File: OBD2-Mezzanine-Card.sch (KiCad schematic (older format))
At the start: 60 parts, among them IC1 ELM327, J1 OBD2-DB9_Male, P1 CONN_02X20, Q1 2N3904, Q2 2N3906, Q3 2N3906, Q4 2N3904, Q5 2N3904, Q6 2N3904, Q7 2N3904, U1 MCP2561-E/P, U2 LM317L_TO92, Y1 4.0MHz

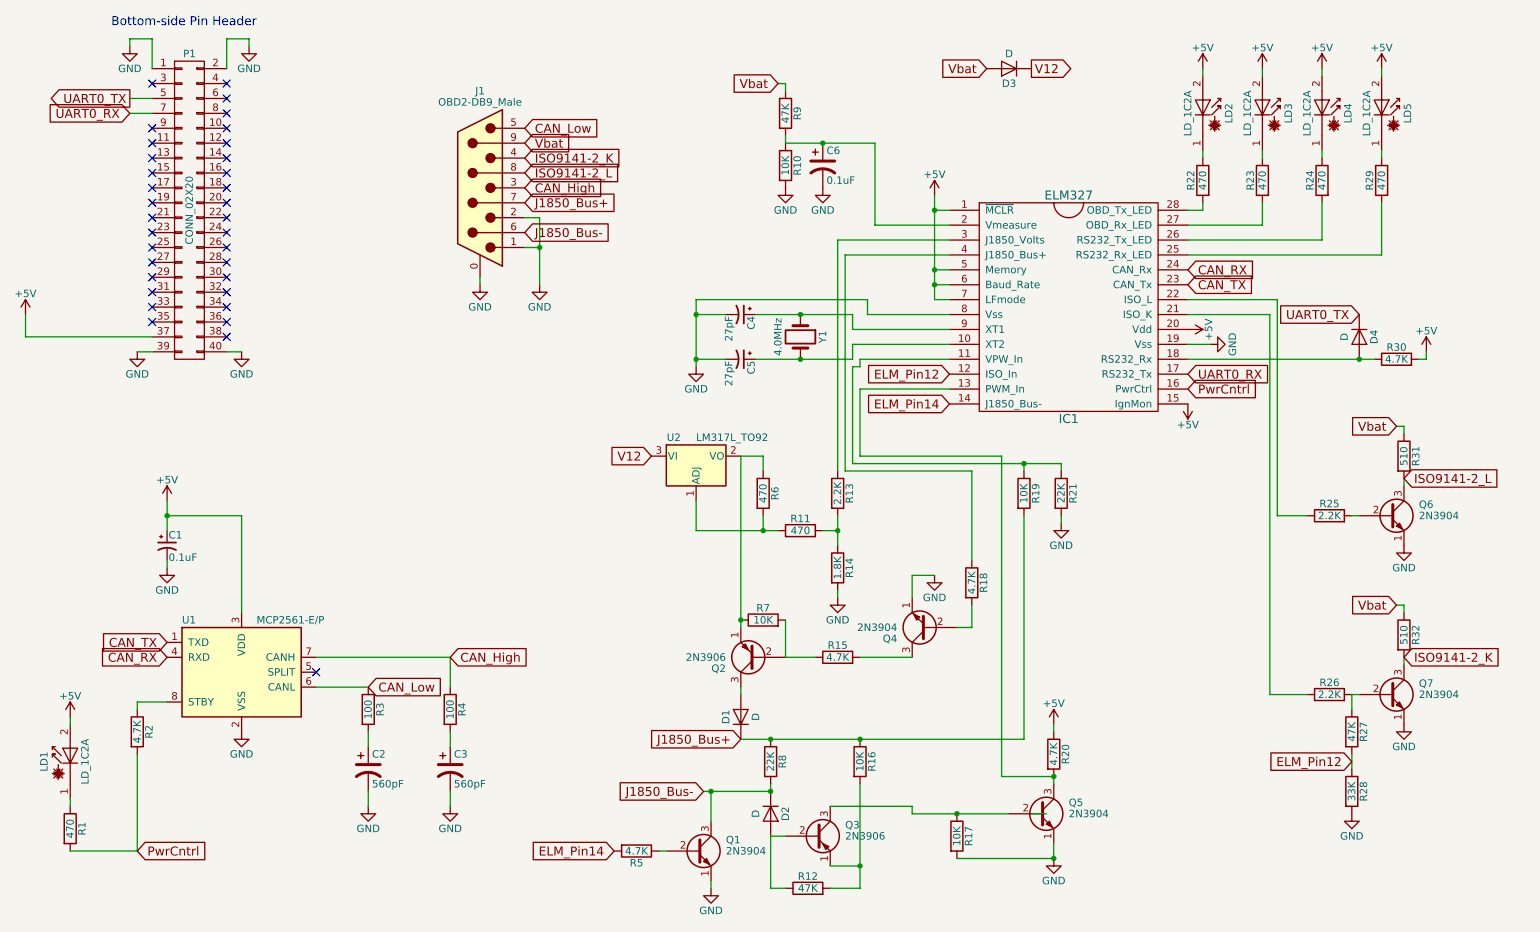
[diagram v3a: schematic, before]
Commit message: sch: Pass all electrical checks and add some lables
Schematic is ready for review.

Signed-off-by: Alistair Francis <alistair@alistair23.me>
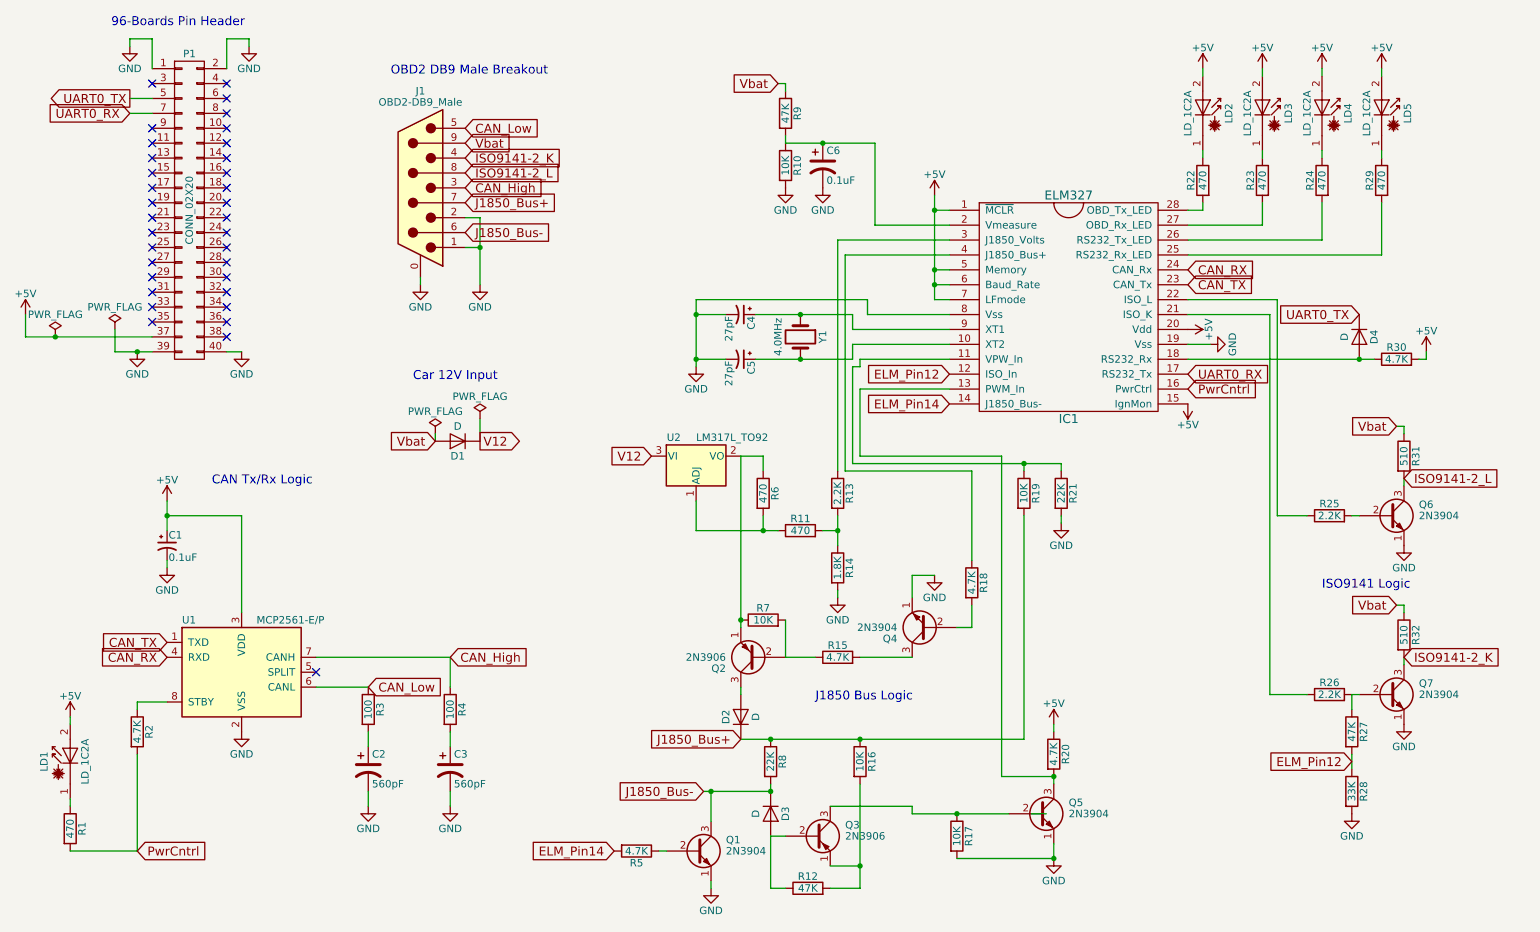
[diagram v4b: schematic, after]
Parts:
- renumbered D3 to D1, D1 to D2, D2 to D3
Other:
- note added: "96-Boards Pin Header"
- note added: "CAN Tx/Rx Logic\n"
- note added: "Car 12V Input\n"
- note added: "ISO9141 Logic\n"
- note added: "J1850 Bus Logic\n"
- note added: "OBD2 DB9 Male Breakout\n"
- note removed: "Bottom-side Pin Header"
- moved on the sheet: D1, J1

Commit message: sch: Add PCB footprints to most parts
Signed-off-by: Alistair Francis <alistair@alistair23.me>
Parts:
- C1, C2, C3, C4, C5, C6: footprint (none) -> Capacitors_SMD:C_0603_HandSoldering
- D1, D2, D3, D4: footprint (none) -> Diodes_SMD:D_SOD-123
- IC1: footprint (none) -> Pin_Headers:Pin_Header_Straight_1x28_Pitch2.54mm
- LD1, LD2, LD3, LD4, LD5: footprint (none) -> Opto-Devices:LaserDiode_TO5(D9)-3
- R1, R11, R22, R23, R24, R29, R3, R31, R32, R4, R6: footprint (none) -> Resistors_SMD:R_0603_HandSoldering
- R10, R12, R16, R17, R19, R21, R27, R28, R7, R8, R9: footprint (none) -> Resistors_SMD:R_1206_HandSoldering
- R13, R14, R15, R18, R2, R20, R25, R26, R30, R5: footprint (none) -> Resistors_SMD:R_0201
- Y1: footprint (none) -> Crystals:Crystal_HC49-U_Vertical

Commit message: sch: Finalise the PCB footprints
Signed-off-by: Alistair Francis <alistair@alistair23.me>
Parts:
- J1: footprint (none) -> Connectors_DSub:DSUB-9_Male_Horizontal_Pitch2.77x2.84mm_EdgePinOffset4.94mm_Housed_MountingHolesOffset7.48mm
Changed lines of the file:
@@
 F 0 "J1" H 3350 2450 50  0000 C CNN
 F 1 "OBD2-DB9_Male" H 3350 2375 50  0000 C CNN
-F 2 "" H 3350 1800 50  0001 C CNN
+F 2 "Connectors_DSub:DSUB-9_Male_Horizontal_Pitch2.77x2.84mm_EdgePinOffset4.94mm_Housed_MountingHolesOffset7.48mm" H 3350 1800 50  0001 C CNN
 F 3 "" H 3350 1800 50  0001 C CNN
 	1    3350 1800

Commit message: sch: Fix up the some PCB footprints
Signed-off-by: Alistair Francis <alistair@alistair23.me>
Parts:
- IC1: footprint Pin_Headers:Pin_Header_Straight_1x28_Pitch2.54mm -> Housings_DIP:DIP-28_W7.62mm
- LD1, LD2, LD3, LD4, LD5: footprint Opto-Devices:LaserDiode_TO5(D9)-3 -> Opto-Devices:LaserDiode_TO3.3(D3.3)-3
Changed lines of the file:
@@
 F 0 "IC1" H 7700 1850 60  0000 C CNN
 F 1 "ELM327" H 7700 3350 60  0000 C CNN
-F 2 "Pin_Headers:Pin_Header_Straight_1x28_Pitch2.54mm" H 7700 3350 60  0001 C CNN
+F 2 "Housings_DIP:DIP-28_W7.62mm" H 7700 3350 60  0001 C CNN
 F 3 "" H 7700 3350 60  0001 C CNN
 	1    7700 2600
@@
 F 0 "LD2" H 8550 1425 50  0000 C CNN
 F 1 "LD_1C2A" H 8550 1150 50  0000 C CNN
-F 2 "Opto-Devices:LaserDiode_TO5(D9)-3" H 8500 1225 50  0001 C CNN
+F 2 "Opto-Devices:LaserDiode_TO3.3(D3.3)-3" H 8500 1225 50  0001 C CNN
 F 3 "" H 8630 1050 50  0001 C CNN
 	1    8600 1250
@@
 F 0 "LD3" H 8950 1425 50  0000 C CNN
 F 1 "LD_1C2A" H 8950 1150 50  0000 C CNN
-F 2 "Opto-Devices:LaserDiode_TO5(D9)-3" H 8900 1225 50  0001 C CNN
+F 2 "Opto-Devices:LaserDiode_TO3.3(D3.3)-3" H 8900 1225 50  0001 C CNN
 F 3 "" H 9030 1050 50  0001 C CNN
 	1    9000 1250
@@
 F 0 "LD4" H 9350 1425 50  0000 C CNN
 F 1 "LD_1C2A" H 9350 1150 50  0000 C CNN
-F 2 "Opto-Devices:LaserDiode_TO5(D9)-3" H 9300 1225 50  0001 C CNN
+F 2 "Opto-Devices:LaserDiode_TO3.3(D3.3)-3" H 9300 1225 50  0001 C CNN
 F 3 "" H 9430 1050 50  0001 C CNN
 	1    9400 1250
@@
 F 0 "LD5" H 9750 1425 50  0000 C CNN
 F 1 "LD_1C2A" H 9750 1150 50  0000 C CNN
-F 2 "Opto-Devices:LaserDiode_TO5(D9)-3" H 9700 1225 50  0001 C CNN
+F 2 "Opto-Devices:LaserDiode_TO3.3(D3.3)-3" H 9700 1225 50  0001 C CNN
 F 3 "" H 9830 1050 50  0001 C CNN
 	1    9800 1250
@@
 F 0 "LD1" H 950 5775 50  0000 C CNN
 F 1 "LD_1C2A" H 950 5500 50  0000 C CNN
-F 2 "Opto-Devices:LaserDiode_TO5(D9)-3" H 900 5575 50  0001 C CNN
+F 2 "Opto-Devices:LaserDiode_TO3.3(D3.3)-3" H 900 5575 50  0001 C CNN
 F 3 "" H 1030 5400 50  0001 C CNN
 	1    1000 5600
